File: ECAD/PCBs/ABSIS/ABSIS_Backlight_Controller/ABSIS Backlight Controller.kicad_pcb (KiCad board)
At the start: 2 copper layers, 101.6 x 53.3 mm, 43 parts, among them J1 PWR IN, J10 BL #9, J11 BL #10, J12 BL #11, J13 BL #12, J2 BL #1, J3 BL #2, J4 BL #3, J5 BL #4, J6 BL #5, J7 BL #6, J8 BL #7, J9 BL #8, P1 Digital, P2 Power, P3 Analog, P4 Analog, P5 PWM, P6 PWM, P7 Communication

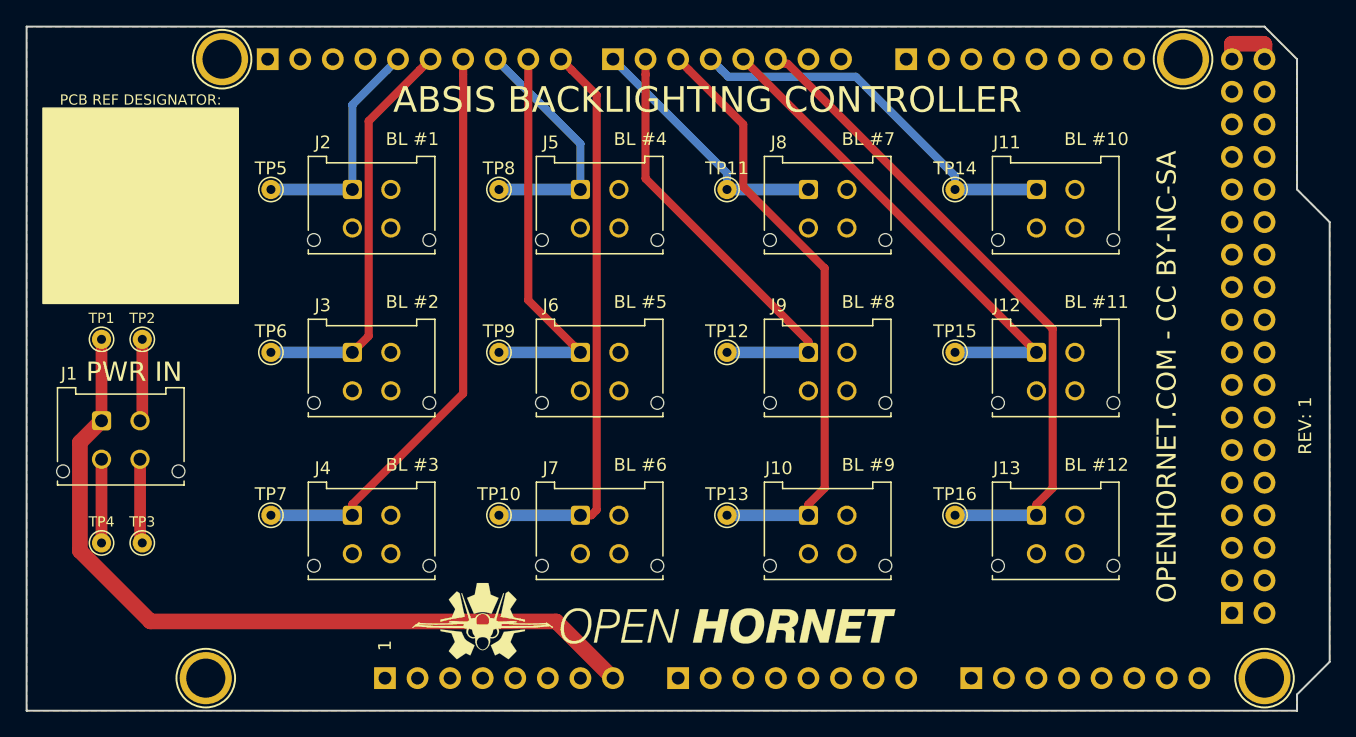
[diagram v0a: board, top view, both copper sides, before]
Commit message: Added ABSIS backlighting controller.
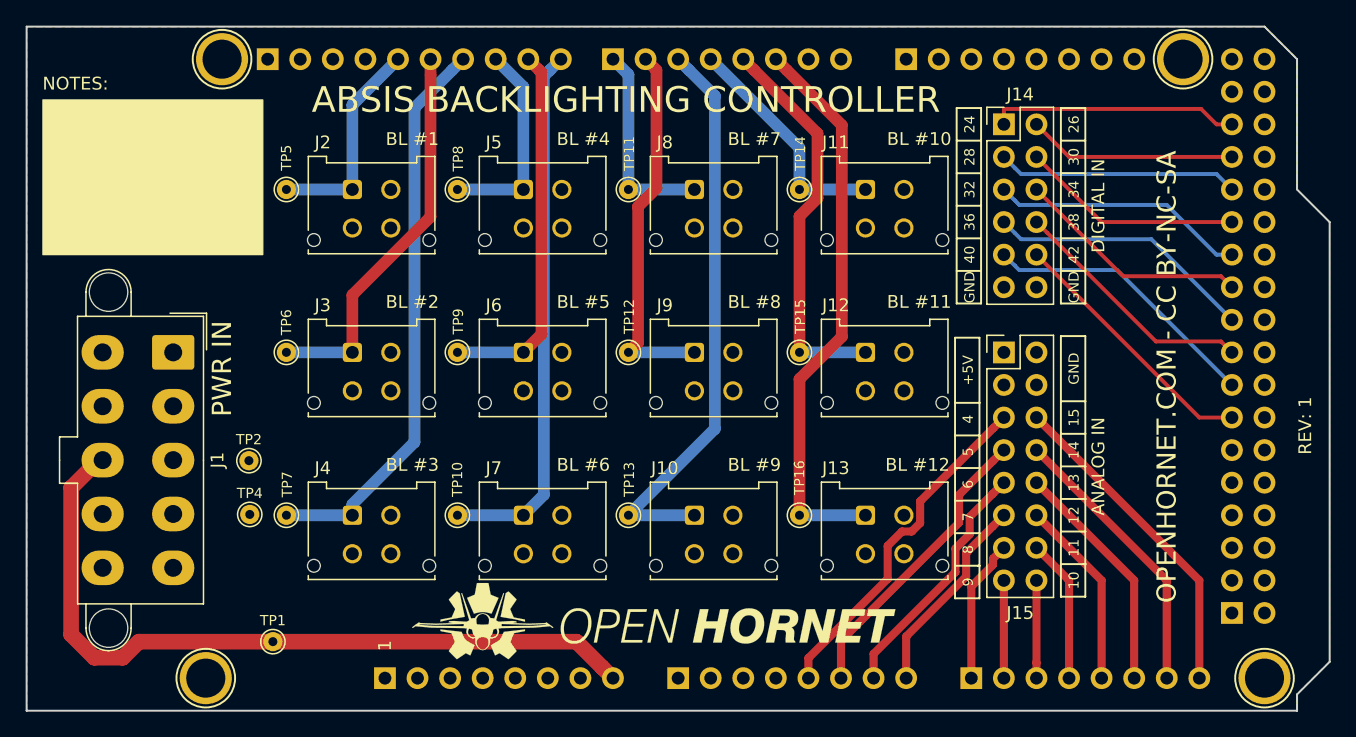
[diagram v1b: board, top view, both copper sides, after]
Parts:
- removed TP3: TP-3.3V, TestPoint:TestPoint_THTPad_D1.5mm_Drill0.7mm
- added J14: DIGITAL IN, Connector_PinHeader_2.54mm:PinHeader_2x06_P2.54mm_Vertical, F.Cu at (179.6, 75.9)
- added J15: ANALOG IN, Connector_PinHeader_2.54mm:PinHeader_2x08_P2.54mm_Vertical, F.Cu at (179.6, 93.7)
- J1: footprint Connector_Molex:Molex_Micro-Fit_3.0_43045-0412_2x02_P3.00mm_Vertical -> Connector_Molex:Molex_Mini-Fit_Jr_5566-10A2_2x05_P4.20mm_Vertical
- moved TP1 27.1 mm to (122.6, 116.3)
- moved J11 13.3 mm to (168.8, 81.0)
- moved J12 13.3 mm to (168.8, 93.7)
- moved J13 13.3 mm to (168.8, 106.4)
- moved TP2 12.6 mm to (120.7, 102.2)
- moved TP14 12.1 mm to (163.6, 81.0)
- moved TP15 12.1 mm to (163.6, 93.7)
- moved TP16 12.1 mm to (163.6, 106.4)
- moved TP4 11.8 mm to (120.8, 106.4)
- moved J10 8.89 mm to (155.4, 106.4)
- moved J8 8.89 mm to (155.4, 81.0)
- moved J9 8.89 mm to (155.4, 93.7)
- moved J1 7.73 mm to (114.8, 93.7), turned to 270 degrees
- moved TP11 7.68 mm to (150.3, 81.0)
- moved TP12 7.68 mm to (150.3, 93.7)
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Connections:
- J1 pad 1: /+12V_SUPPLY -> /+5V_SUPPLY
- J1 pad 3: GND -> /+5V_SUPPLY
- J1 pad 4: /+3.3V_SUPPLY -> GND
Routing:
- net /A4: track 0.00 -> 27.1 mm
- net /A15: track 0.00 -> 25.6 mm
- net /A5: track 0.00 -> 23.0 mm
- net /40: track 0.00 -> 22.0 mm
- net /A14: track 0.00 -> 22.0 mm
- net /36: track 0.00 -> 20.9 mm
- net /42: track 0.00 -> 20.5 mm
- net /32: track 0.00 -> 19.9 mm
- net /24: track 0.00 -> 19.5 mm
- net /A6: track 0.00 -> 19.4 mm
- net /38: track 0.00 -> 19.4 mm
- net /28: track 0.00 -> 18.8 mm
- net /A13: track 0.00 -> 18.4 mm
- net /34: track 0.00 -> 18.4 mm
- net /30: track 0.00 -> 17.3 mm
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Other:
- board text added: "+5V"
- board text added: "10"
- board text added: "11"
- board text added: "12"
- board text added: "13"
- board text added: "14"
- board text added: "15"
- board text added: "24"
- board text added: "26"
- board text added: "28"
- board text added: "30"
- board text added: "32"
- board text added: "34"
- board text added: "36"
- board text added: "38"
- board text added: "4"
- board text added: "40"
- board text added: "42"
- board text added: "5"
- board text added: "6"
- board text added: "7"
- board text added: "8"
- board text added: "9"
- board text added: "GND"
- board text added: "NOTES:"
- board text removed: "PCB REF DESIGNATOR:"
